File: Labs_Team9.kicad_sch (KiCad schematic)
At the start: 14 parts, among them J1 Conn_02x04_Counter_Clockwise, SW1 SW_Push, SW2 SW_Push, U1 STM32F411RETx, Y1 Crystal_GND24

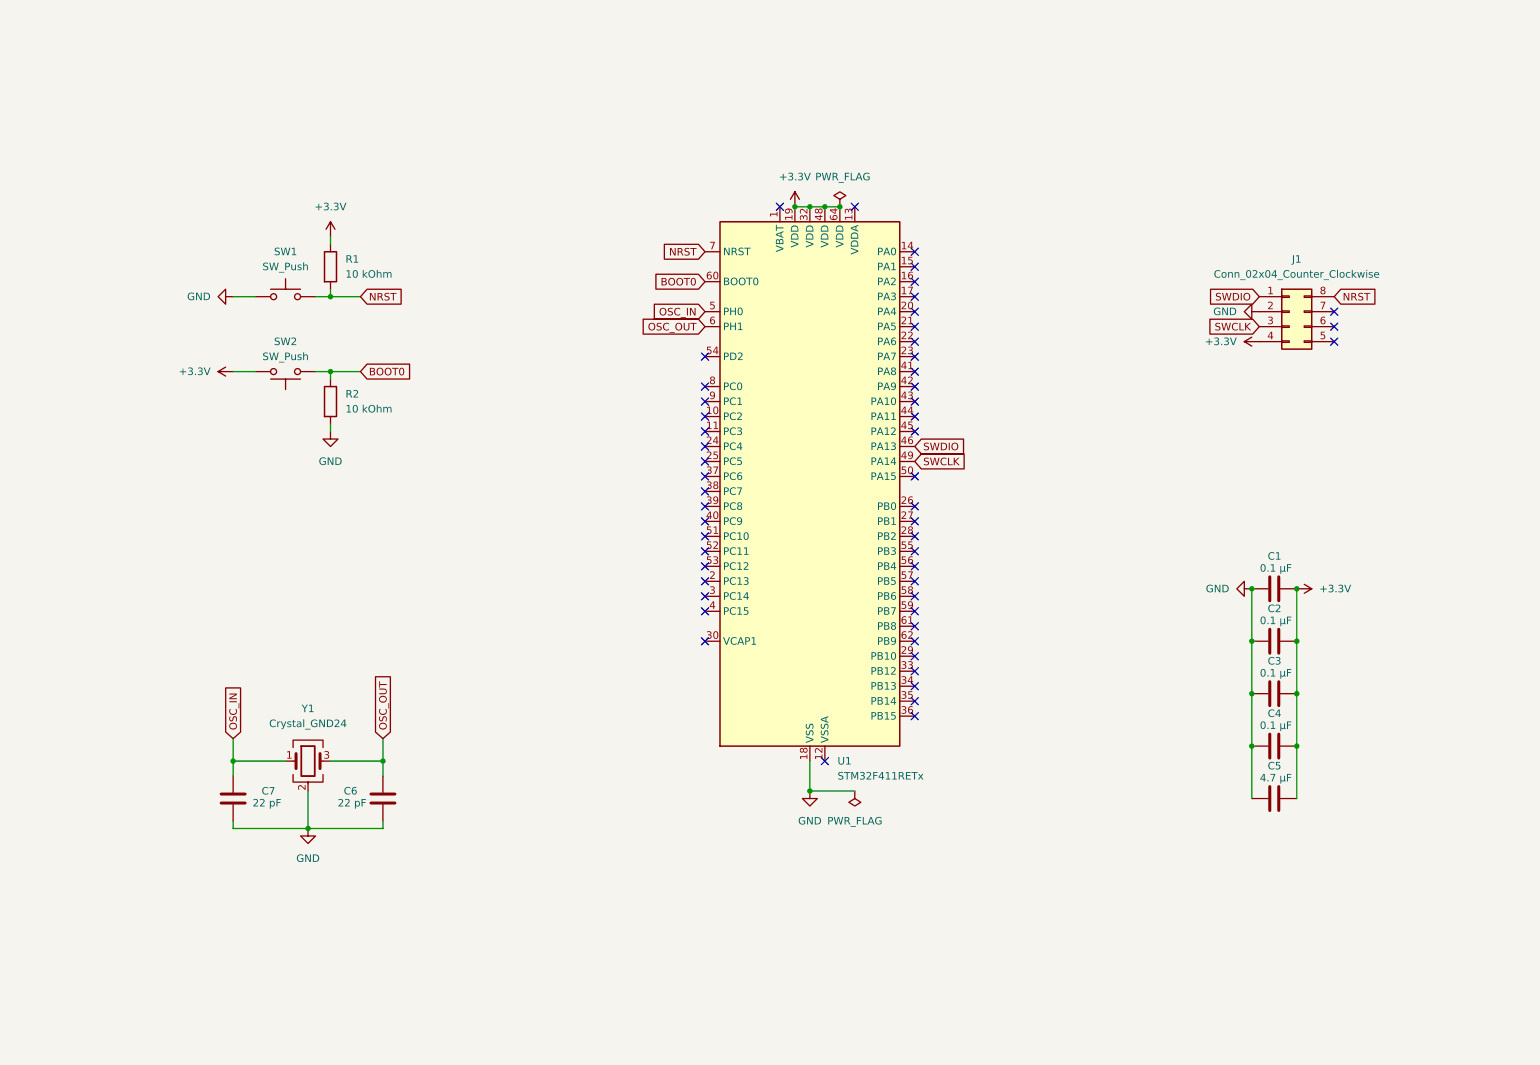
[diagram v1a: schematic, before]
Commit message: lab2: add schematic and part of the trace
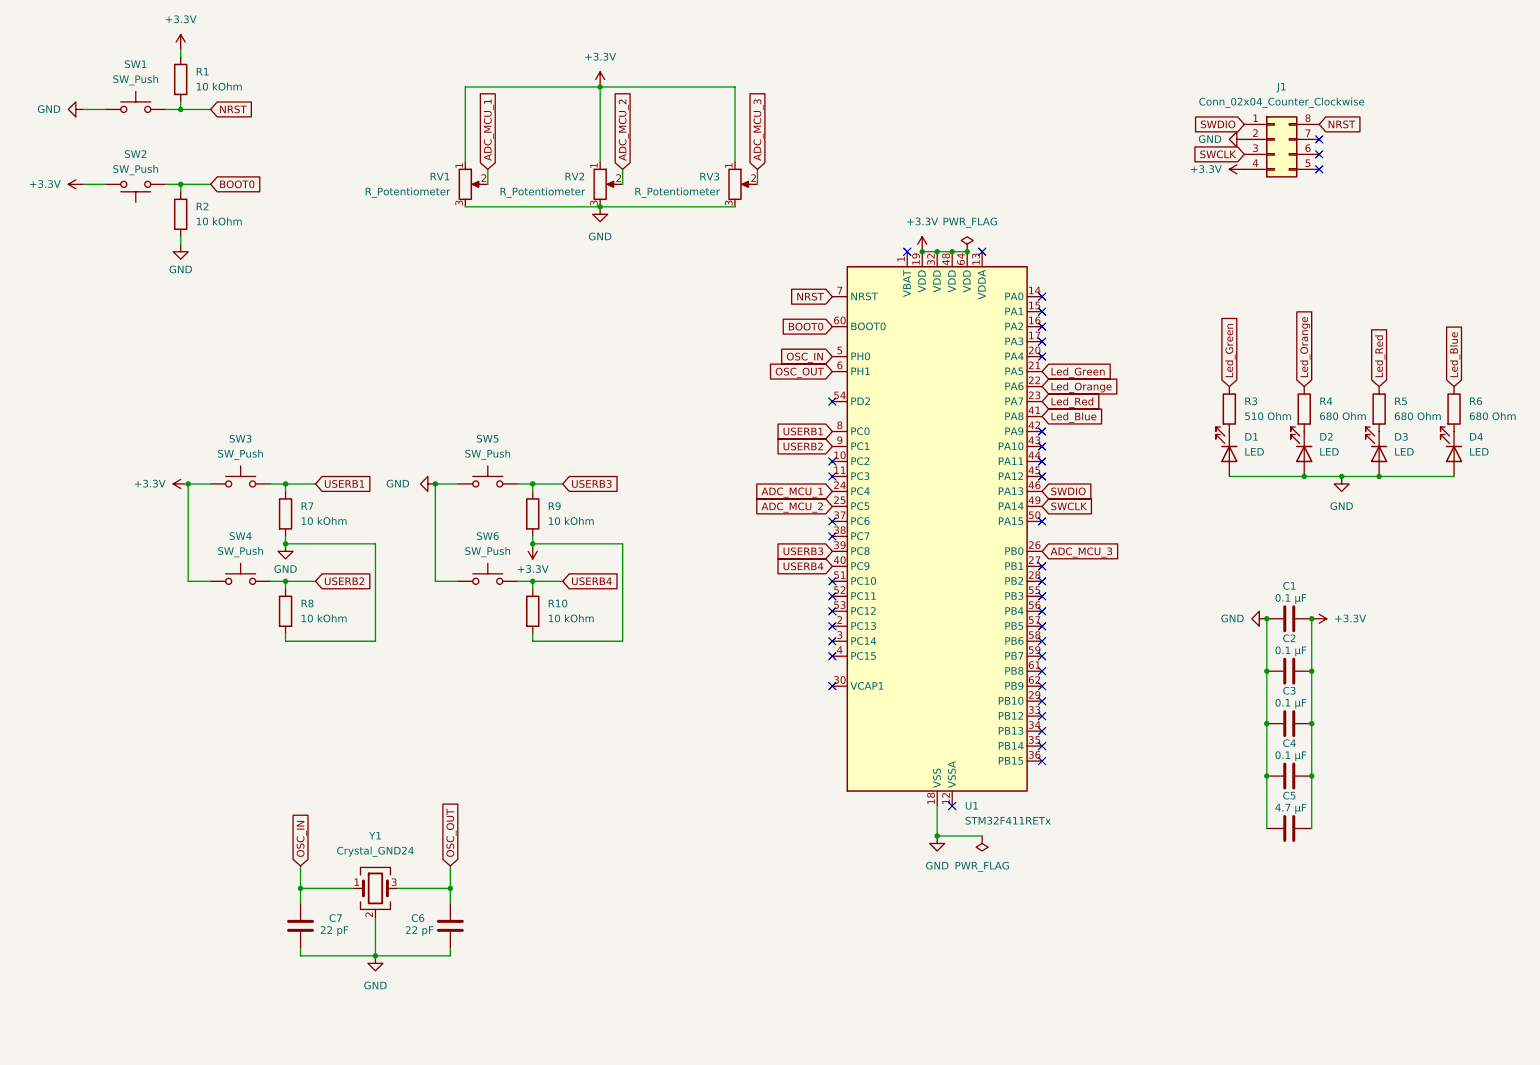
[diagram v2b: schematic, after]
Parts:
- added D1, D2, D3, D4: LED, LED_SMD:LED_1206_3216Metric_Pad1.42x1.75mm_HandSolder, symbol Device:LED
- added R10, R7, R8, R9: 10 kOhm, Resistor_SMD:R_1206_3216Metric_Pad1.30x1.75mm_HandSolder, symbol Device:R
- added R3: 510 Ohm, Resistor_SMD:R_1206_3216Metric_Pad1.30x1.75mm_HandSolder, symbol Device:R
- added R4, R5, R6: 680 Ohm, Resistor_SMD:R_1206_3216Metric_Pad1.30x1.75mm_HandSolder, symbol Device:R
- added RV1, RV2, RV3: R_Potentiometer, Potentiometer_THT:Potentiometer_Bourns_3339P_Vertical_HandSoldering, symbol Device:R_Potentiometer
- added SW3, SW4, SW5, SW6: SW_Push, Buttons_Switches_THT:SW_PUSH_6mm, symbol Switch:SW_Push
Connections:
- net +3.3V: now also R10.2, R9.2, RV1.1, RV2.1, RV3.1, SW3.1, SW4.1
- net GND: now also D1.2 (A), D2.2 (A), D3.2 (A), D4.2 (A), R7.2, R8.2, RV1.3, RV2.3, RV3.3, SW5.1, SW6.1
- net Led_Green: now reaches U1.21 (PA5)
- net Led_Green: now also R3.1
- net Led_Orange: now reaches U1.22 (PA6)
- net Led_Orange: now also R4.1
- net Led_Red: now reaches U1.23 (PA7)
- net Led_Red: now also R5.1
- net ADC_MCU_1: now reaches U1.24 (PC4)
- net ADC_MCU_1: now also RV1.2
- net ADC_MCU_2: now reaches U1.25 (PC5)
- net ADC_MCU_2: now also RV2.2
- net ADC_MCU_3: now reaches U1.26 (PB0)
- net ADC_MCU_3: now also RV3.2
- net USERB3: now reaches U1.39 (PC8)
- net USERB3: now also R9.1, SW5.2
- net USERB4: now reaches U1.40 (PC9)
- net USERB4: now also R10.1, SW6.2
- net Led_Blue: now reaches U1.41 (PA8)
- net Led_Blue: now also R6.1
- net USERB1: now reaches U1.8 (PC0)
- net USERB1: now also R7.1, SW3.2
- net USERB2: now reaches U1.9 (PC1)
- net USERB2: now also R8.1, SW4.2
- new net: D1.1 (K), R3.2
- new net: D4.1 (K), R6.2
- new net: D3.1 (K), R5.2
- new net: D2.1 (K), R4.2
- no-connect marks 53 -> 42
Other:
- title: (none) -> Labs_Team9
- moved on the sheet: C1, C2, C3, C4, C5, C6, C7, J1, R1, R2, SW1, SW2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

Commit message: lab3: add schematic
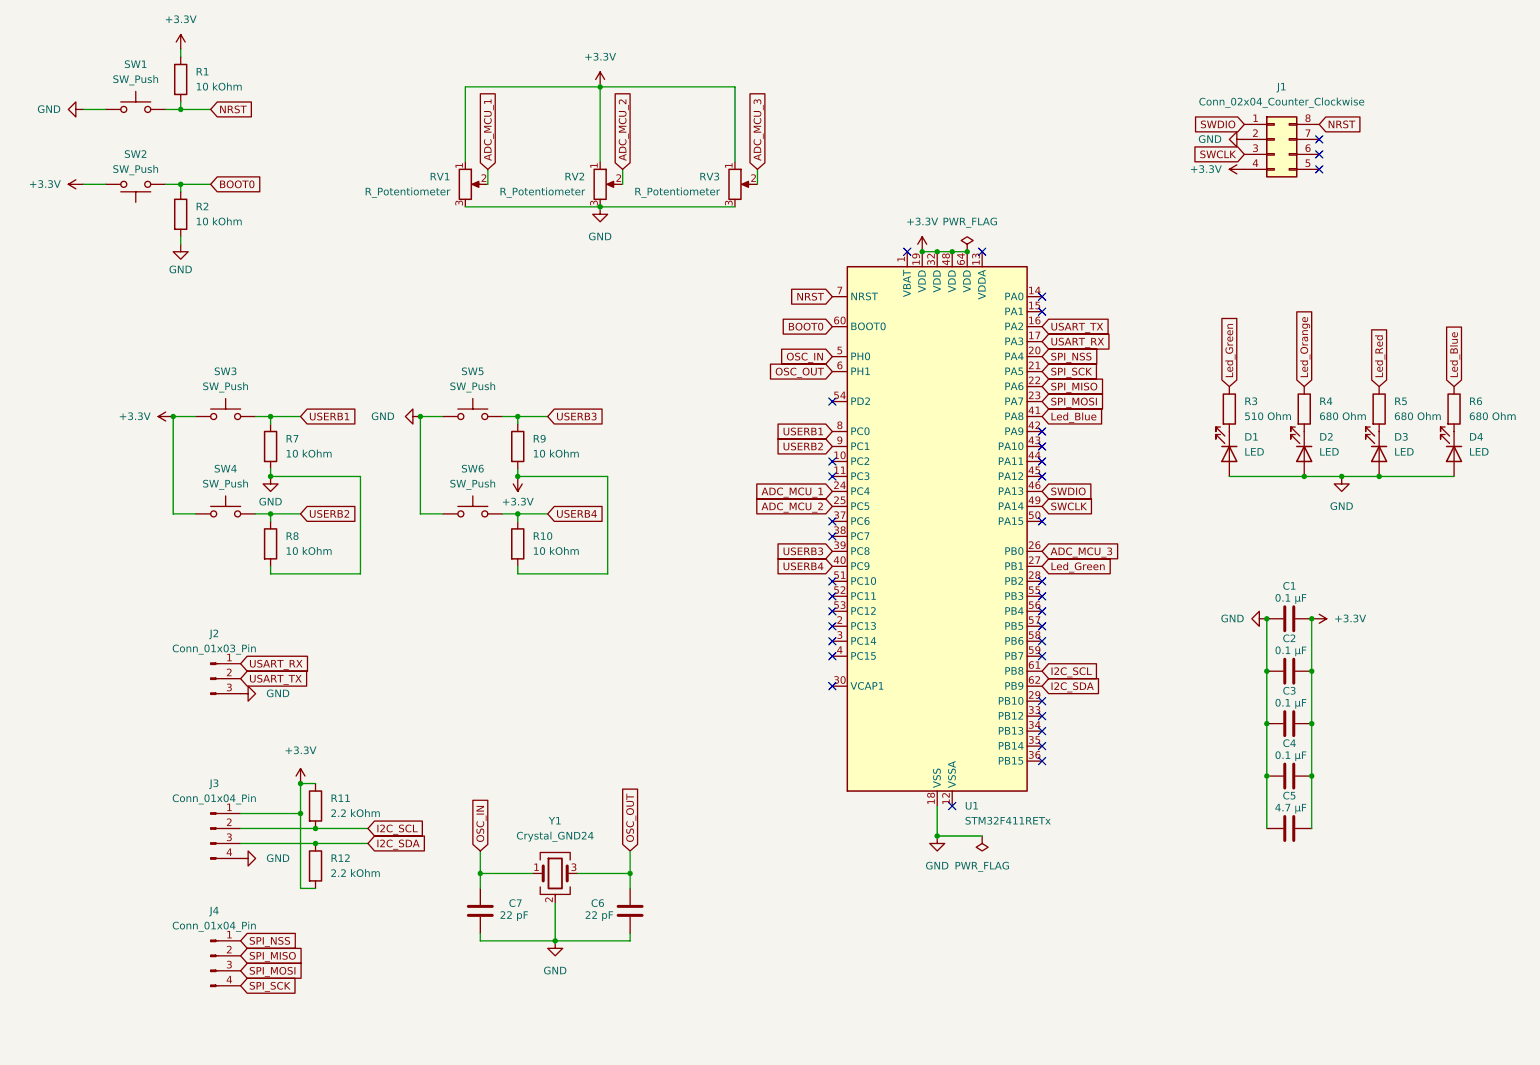
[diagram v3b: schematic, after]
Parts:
- added J2: Conn_01x03_Pin, Connector_PinHeader_2.54mm:PinHeader_1x03_P2.54mm_Vertical, symbol Connector:Conn_01x03_Pin
- added J3, J4: Conn_01x04_Pin, Connector_PinHeader_2.54mm:PinHeader_1x04_P2.54mm_Vertical, symbol Connector:Conn_01x04_Pin
- added R11, R12: 2.2 kOhm, Resistor_SMD:R_1206_3216Metric_Pad1.30x1.75mm_HandSolder, symbol Device:R
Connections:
- net +3.3V: now also J3.1 (Pin_1), R11.1, R12.2
- net GND: now also J2.3 (Pin_3), J3.4 (Pin_4)
- net Led_Green: now also U1.27 (PB1); no longer U1.21 (PA5)
- net Led_Orange: no longer U1.22 (PA6)
- net Led_Red: no longer U1.23 (PA7)
- net USART_TX: now reaches U1.16 (PA2)
- net USART_TX: now also J2.2 (Pin_2)
- net USART_RX: now reaches U1.17 (PA3)
- net USART_RX: now also J2.1 (Pin_1)
- net SPI_NSS: now reaches U1.20 (PA4)
- net SPI_NSS: now also J4.1 (Pin_1)
- net I2C_SCL: now reaches U1.61 (PB8)
- net I2C_SCL: now also J3.2 (Pin_2), R11.2
- net I2C_SDA: now reaches U1.62 (PB9)
- net I2C_SDA: now also J3.3 (Pin_3), R12.1
- new net SPI_MISO: J4.2 (Pin_2), U1.22 (PA6)
- new net SPI_MOSI: J4.3 (Pin_3), U1.23 (PA7)
- new net SPI_SCK: J4.4 (Pin_4), U1.21 (PA5)
- no-connect marks 42 -> 36
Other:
- moved on the sheet: C6, C7, R10, R7, R8, R9, SW3, SW4, SW5, SW6, Y1

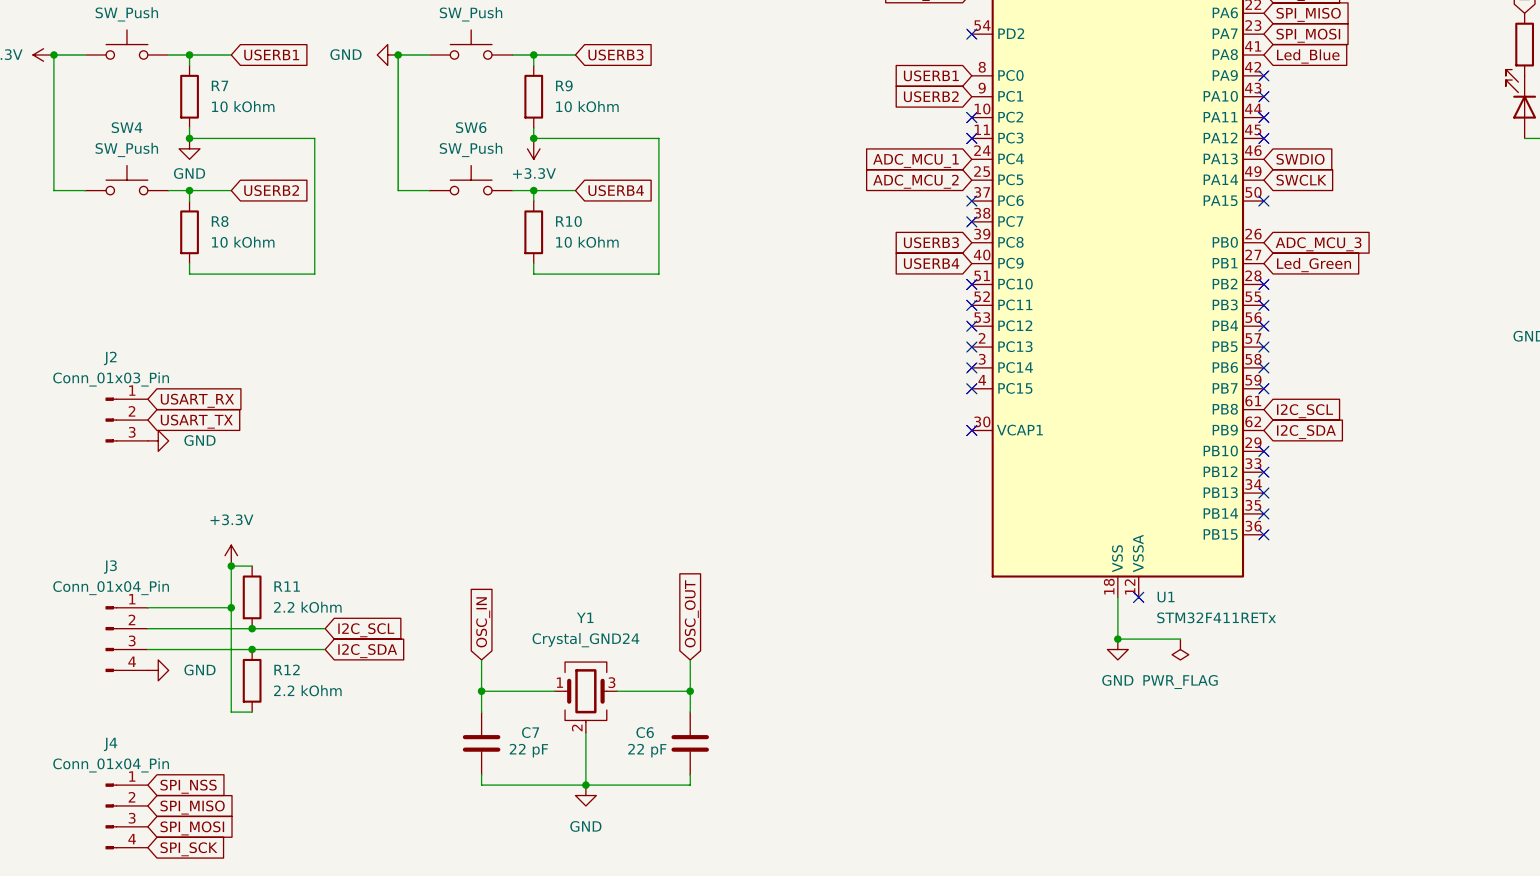
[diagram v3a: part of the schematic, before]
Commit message: lab3: add tracing
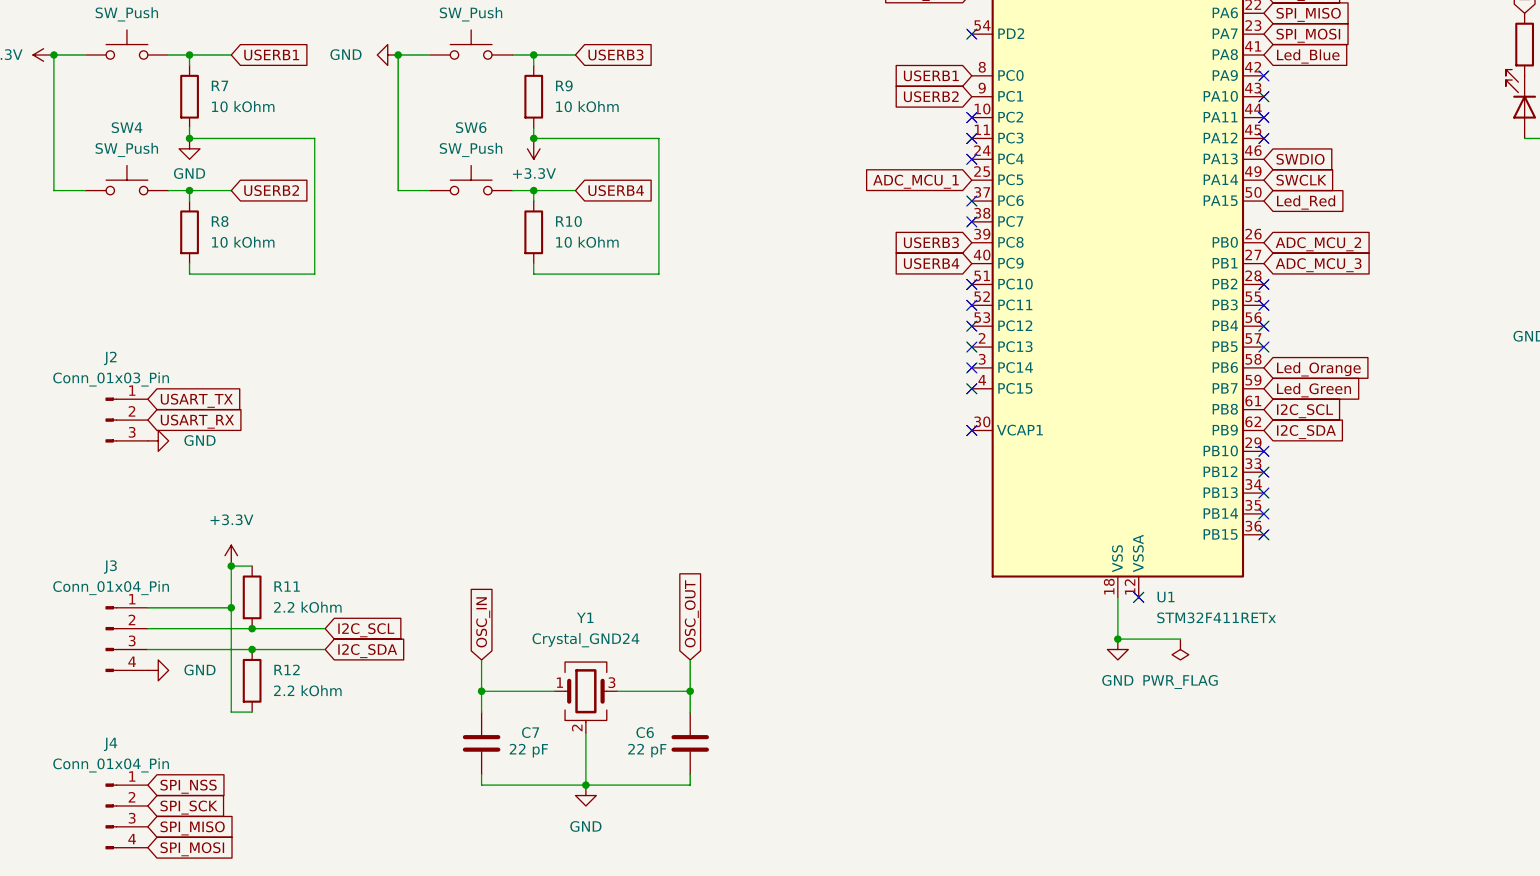
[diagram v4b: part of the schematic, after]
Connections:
- net ADC_MCU_1: now also U1.25 (PC5); no longer U1.24 (PC4)
- net ADC_MCU_2: now also U1.26 (PB0); no longer U1.25 (PC5)
- net ADC_MCU_3: now also U1.27 (PB1); no longer U1.26 (PB0)
- net Led_Green: now also U1.59 (PB7); no longer U1.27 (PB1)
- net Led_Orange: now also U1.58 (PB6)
- net Led_Red: now also U1.50 (PA15)
- net SPI_MISO: now also J4.3 (Pin_3); no longer J4.2 (Pin_2)
- net SPI_MOSI: now also J4.4 (Pin_4); no longer J4.3 (Pin_3)
- net SPI_SCK: now also J4.2 (Pin_2); no longer J4.4 (Pin_4)
- net USART_RX: now also J2.2 (Pin_2); no longer J2.1 (Pin_1)
- net USART_TX: now also J2.1 (Pin_1); no longer J2.2 (Pin_2)
- no-connect marks 36 -> 34
